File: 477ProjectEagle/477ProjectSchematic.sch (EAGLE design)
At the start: 42 parts, among them Q1 AO4419, X10 22-23-2041, X9 22-23-2041

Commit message: Updated schematic
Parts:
- removed FUELGUAGE: 22-23-2021, con-molex:22-23-2021
- removed X9: 22-23-2041, con-molex:22-23-2041
- added SW_1: RESET_BUTTON, MinotaurParts:RESET_BUTTON
- added U$19: TXB0108, MinotaurParts:TXB0108
- added U$20: 10k, MinotaurParts:R-US
- added U$21: 1k, MinotaurParts:R-US
- added U$22: (no value), MinotaurParts:R-US
- added X1: 22-23-2051, con-molex:22-23-2051
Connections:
- new net N$17: U$1.PMD3/RE3, U$19.A2
- new net N$32: U$1.PMD1/RE1, U$19.A4
- new net N$34: U$1.OC3/RD2, U$19.A5
- new net N$38: U$1.OC2/RD1, U$19.A6
- new net N$39: U$19.B1, U$2.IN1
- new net N$41: U$19.B4, U$2.IN4
- new net N$42: U$19.B2, U$2.IN2
- new net N$43: U$19.B3, U$2.IN3
- new net N$44: U$19.B5, U$2.ENA
- new net N$45: U$19.B6, U$2.ENB
- new net N$46: U$19.VCCA
- new net N$47: U$19.B7, U$39.R1OUT
- new net N$49: U$19.B8, U$39.T1IN
- new net N$50: U$39.T1OUT
- new net N$53: U$39.R1IN
- new net N$56: U$19.OE, U$20.1
- new net N$57: U$20.2
- new net N$58: U$1.*MCLR, U$21.2, U$22.1
- new net N$60: SW_1.2, U$21.1
- new net N$62: U$22.2
- net +5V: now also U$19.VCCB
- net +7V: now also U$2.VS; no longer X10-3.S, X9-3.S
- net GND: now also SW_1.1, U$1.VSS, U$1.VSS_2, U$1.VSS_3, U$19.GND, U$2.VSS
- net N$14: now also U$1.PGC1/EMUC1/VREF-/AN1/CN3/RB1; no longer U$1.VSS_2
- net N$15: now also U$1.PMD4/RE4, U$19.A1; no longer U$1.VSS
- net N$19: now also U$2.OUT2
- net N$20: now also X10-3.S; no longer X9-1.S
- net N$21: now also U$2.OUT3, X10-4.S; no longer X9-2.S
- net N$23: no longer FUELGUAGE-1.S
- net N$24: no longer FUELGUAGE-2.S
- net N$29: now also U$1.PMD2/RE2, U$19.A3; no longer U$2.VS
- net N$7: now also U$1.PGD1/EMUD1/PMA6/VREF+/AN0/CN2/RB0; no longer U$1.VSS_3
- net N$8: now also U$19.A7; no longer U$39.R1OUT
- net N$9: now also U$19.A8; no longer U$39.T1IN
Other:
- note added: "3.3Volt!"
- note added: "TO MOTORS"
- moved on the sheet: Q1, U$10, U$11, U$12, U$13, U$14, U$15, U$16, U$17, U$18, U$2, U$26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

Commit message: Fixed Schematic
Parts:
- added J1: POWER_JACKPTH, SparkFun-Connectors:POWER_JACKPTH
- added SV1: (no value), con-lsta:FE08-1
- added SV2: (no value), con-lsta:FE09-1
- added SV3, SV4: (no value), con-lsta:FE10-1
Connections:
- new net N$13: U$1.SDA1/RG3
- new net N$31: U$1.PMA8/U2TX/SCL2/CN18/RF5
- new net N$61: SV2.4, U$1.TDI/PMA10/AN13/RB13
- new net N$63: U$1.TDO/PMA12/AN11/RB11
- new net N$64: SV2.7, U$1.TMS/PMA13/CVREF/AN10/RB10
- new net N$65: U$1.*U2CTS/C1OUT/AN8/RB8
- new net N$66: U$1.PGD2/EMUD2/AN7/RB7
- new net N$67: SV4.10, U$1.*U1RTS/BCLK1/SCK1/INT0/RF6
- new net N$68: U$1.OSC1/CLKI/RC12
- new net N$69: U$1.IC1/RTCC/INT1/RD8
- new net N$70: SV4.6, U$1.IC2/*U1CTS/INT2/RD9
- new net N$71: SV4.5, U$1.IC3/PMCS2/INT3/RD10
- new net N$72: SV4.4, U$1.IC4/PMCS1/INT4/RD11
- new net N$73: SV4.3, U$1.OC1/RD0
- new net N$74: U$1.SOSCI/CN1/RC13
- new net N$75: U$1.SOSCO/T1CK/CN0/RC14
- new net N$76: SV3.1, U$1.PMD0/RE0
- new net N$77: SV3.2
- new net N$78: SV3.3
- new net N$79: SV3.4
- new net N$80: SV3.5
- new net N$81: SV3.6
- new net N$82: SV3.7, U$1.CN15/RD6
- new net N$83: SV3.8, U$1.PMRD/CN14/RD5
- new net N$84: SV3.9, U$1.PMWR/OC5/IC5/CN13/RD4
- new net N$85: SV3.10
- new net SCL: ENCODER-1.S, X1-4.S
- new net SDA: ENCODER-2.S, X1-3.S
- new net V+: J1.PWR, U$12.EN, U$12.VIN, U$13.1, U$26.VIN, U$27.1, U$28.2, U$29.1, U$30.2, U$31.1, U$32.2, U$4.VIN, U$5.1
- net +3V3: now also U$1.VDD, U$1.VDD_2, U$1.VDD_3, U$19.VCCA, U$20.2, U$22.2, X1-2.S
- net +5V: now also U$1.AVDD
- net GND: now also J1.GND, J1.GNDBREAK, U$1.AVSS, X1-1.S
- net N$10: now also SV1.7, U$1.PMD6/RE6; no longer U$12.EN, U$12.VIN, U$13.1
- net N$11: now also SV1.6, U$1.PMD7/RE7; no longer U$1.VDD_2
- net N$22: now also U$1.PMA0/AN15/OCFB/CN12/RB15
- net N$23: now also SV1.5, U$1.PMA5/SCK2/CN8/RG6; no longer ENCODER-1.S
- net N$24: now also SV1.4, U$1.PMA4/SDI2/CN9/RG7; no longer ENCODER-2.S
- net N$26: now also SV1.3, U$1.PMA3/SDO2/CN10/RG8; no longer U$26.VIN, U$27.1, U$28.2, U$29.1, U$30.2, U$31.1, U$32.2
- net N$27: now also SV1.2, U$1.PMA2/*SS2/CN11/RG9; no longer U$1.AVDD
- net N$30: now also SV1.1, U$1.PGC2/EMUC2/AN6/OCFA/RB6; no longer U$4.VIN, U$5.1
- net N$46: now also U$1.PMA9/U2RX/SDA2/CN17/RF4; no longer U$19.VCCA
- net N$5: now also U$1.PMA7/C2OUT/AN9/RB9
- net N$57: now also U$1.PMA1/*U2RTS/BCLK2/AN14/RB14; no longer U$20.2
- net N$59: now also U$1.OSC2/CLKO/RC15; no longer U$1.VDD
- net N$6: now also SV1.8, U$1.PMD5/RE5; no longer U$1.VDD_3
- net N$62: now also U$1.TCK/PMA11/AN12/RB12; no longer U$22.2
- net N$9: now also U$1.U1TX/SDO1/RF3
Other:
- note removed: "3.3Volt!"
- moved on the sheet: X1-1, X1-2, X1-3, X1-4

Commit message: Made further edits to both schematics
decoupling capacitors, values for passive components, RJ11 and SUBD
connectors.
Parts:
- added U$23, U$24, U$25, U$40, U$41, U$42, U$43, U$44: 10uF, MinotaurParts:C-US-1206
- added X2: XRJK-S-01-6-6-0-2G2-NO, con-xmultiple:XRJK-S-01-6-6-0-2G2-NO
- added X3: (no value), con-subd:F09HP
- U$11: value APXA100ARA271MJ80G -> 270uF
- U$13: value (none) -> 10uF
- U$14: value (none) -> 22uF
- U$15: value SDR0403 -> 2.2uH
- U$16: value (none) -> 100k; device MinotaurParts:R-US -> MinotaurParts:R-US"
- U$17, U$18, U$20, U$21: device MinotaurParts:R-US -> MinotaurParts:R-US"
- U$22: value (none) -> 5k; device MinotaurParts:R-US -> MinotaurParts:R-US"
- U$27, U$5: value C-US-1210 -> 10uF
- U$28: value (none) -> 110k; device MinotaurParts:R-US -> MinotaurParts:R-US"
- U$29: value (none) -> 740nF
- U$30: value (none) -> 2.55k; device MinotaurParts:R-US -> MinotaurParts:R-US"
- U$31: value (none) -> 1.0nF
- U$32: value (none) -> 0.020; device MinotaurParts:R-US -> MinotaurParts:R-US"
- U$34: value (none) -> 4.7uH
- U$35: value (none) -> 3.9nF
- U$36: value (none) -> 12k; device MinotaurParts:R-US -> MinotaurParts:R-US"
- U$37: value (none) -> 1.4k; device MinotaurParts:R-US -> MinotaurParts:R-US"
- U$38: value T495D336K025ATE090 -> 33uF
- U$6: value (none) -> 10nF
- U$7: value SRR1210 -> 12uH
- U$8: value (none) -> 10k; device MinotaurParts:R-US -> MinotaurParts:R-US"
- U$9: value (none) -> 2.05k; device MinotaurParts:R-US -> MinotaurParts:R-US"
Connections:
- removed net N$50: U$39.T1OUT
- new net N$86: X2.3
- new net N$87: U$39.R1IN, X3.3
- net +3V3: now also U$23.1, U$24.1, U$25.1, U$41.1, U$44.1, X2.2
- net +5V: now also U$15.2, U$40.1, U$42.1, U$43.1; no longer U$15.B
- net +7V: now also U$7.2; no longer U$7.A
- net GND: now also U$23.2, U$24.2, U$25.2, U$40.2, U$41.2, U$42.2, U$43.2, U$44.2, X3.1
- net N$14: now also X2.5
- net N$16: now also U$7.1; no longer U$7.B
- net N$36: now also U$15.1; no longer U$15.A
- net N$53: now also U$39.T1OUT, X3.2; no longer U$39.R1IN
- net N$58: now also X2.1
- net N$7: now also X2.4
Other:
- note added: "PIC24FJ128GA006"
- moved on the sheet: U$12, U$13, U$14, U$15, U$16, U$17, U$18, U$31, U$7

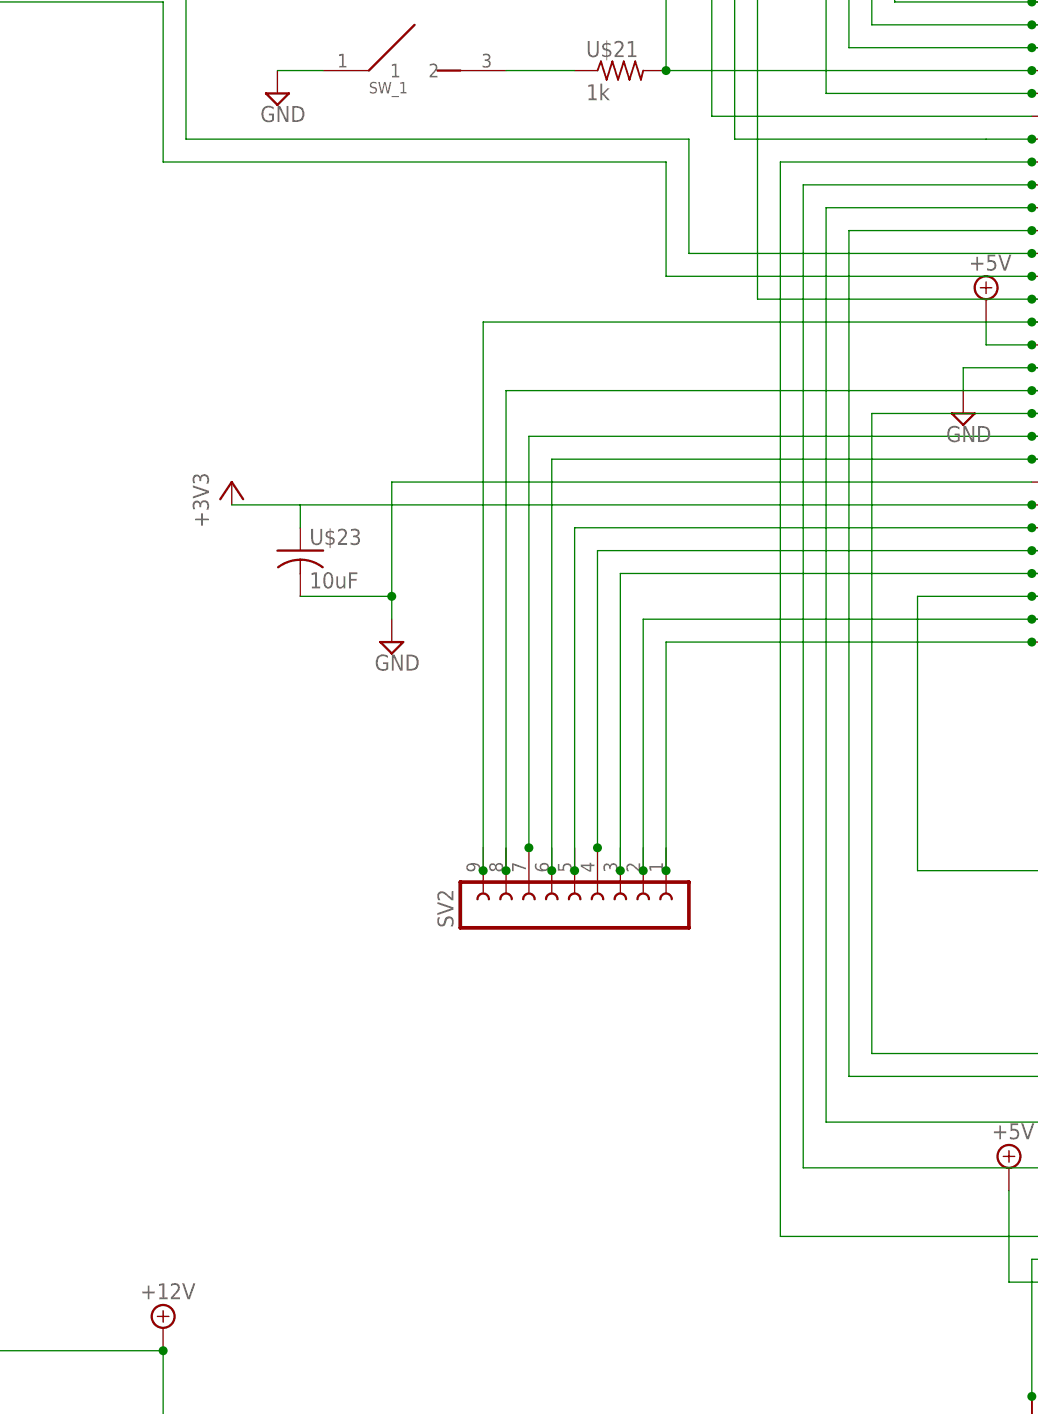
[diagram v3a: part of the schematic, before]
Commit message: Updated micro code and small schematic fix
Added ADC code to micro project. The code initializes adc to capture
data from all 5 sensors the interrupt when done.
Also added decoupling caps to the ADC input lines.
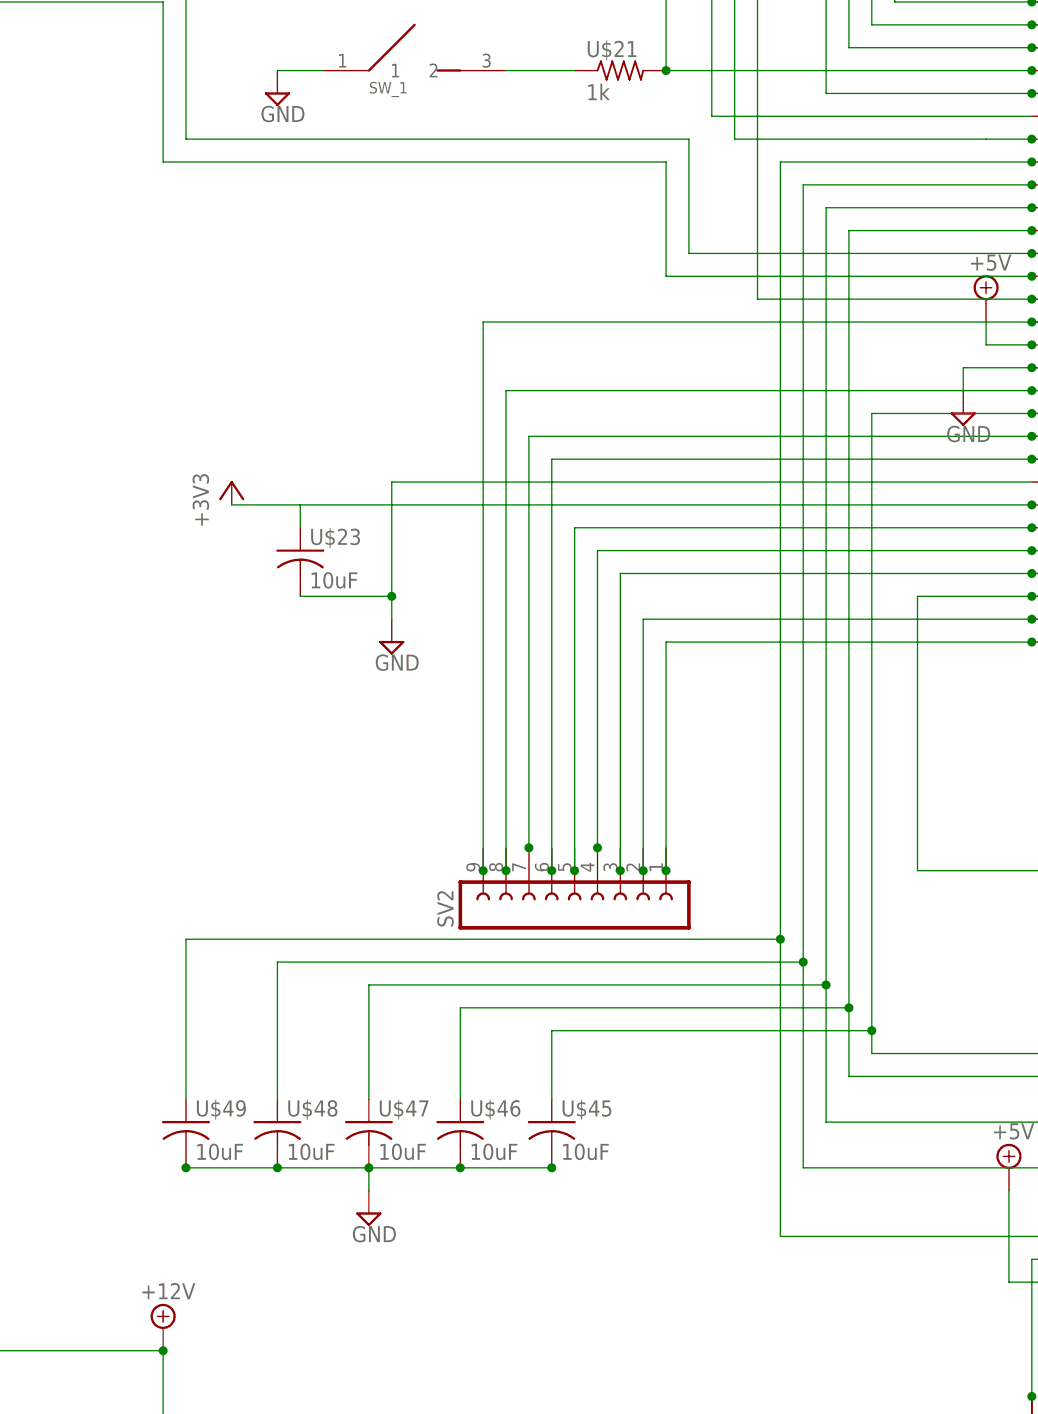
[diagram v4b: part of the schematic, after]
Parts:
- added U$45, U$46, U$47, U$48, U$49: 10uF, MinotaurParts:C-US-1206
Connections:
- net GND: now also U$45.2, U$46.2, U$47.2, U$48.2, U$49.2
- net N$1: now also U$49.1
- net N$2: now also U$48.1
- net N$3: now also U$47.1
- net N$4: now also U$46.1
- net N$5: now also U$45.1
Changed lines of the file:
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@@
 <part name="X3" library="con-subd" deviceset="F09" device="HP"/>
 <part name="SUPPLY47" library="supply2" deviceset="GND" device=""/>
+<part name="U$45" library="MinotaurParts" deviceset="C-US-1206" device="" value="10uF"/>
+<part name="U$46" library="MinotaurParts" deviceset="C-US-1206" device="" value="10uF"/>
+<part name="U$47" library="MinotaurParts" deviceset="C-US-1206" device="" value="10uF"/>
+<part name="U$48" library="MinotaurParts" deviceset="C-US-1206" device="" value="10uF"/>
+<part name="U$49" library="MinotaurParts" deviceset="C-US-1206" device="" value="10uF"/>
+<part name="SUPPLY48" library="supply2" deviceset="GND" device=""/>
 </parts>
 <sheets>
@@
 <instance part="X3" gate="G$1" x="248.92" y="25.4"/>
 <instance part="SUPPLY47" gate="GND" x="236.22" y="35.56"/>
+<instance part="U$45" gate="G$1" x="-132.08" y="-83.82"/>
+<instance part="U$46" gate="G$1" x="-142.24" y="-83.82"/>
+<instance part="U$47" gate="G$1" x="-152.4" y="-83.82"/>
+<instance part="U$48" gate="G$1" x="-162.56" y="-83.82"/>
+<instance part="U$49" gate="G$1" x="-172.72" y="-83.82"/>
+<instance part="SUPPLY48" gate="GND" x="-152.4" y="-93.98"/>
 </instances>
 <busses>
@@
 <pinref part="U$1" gate="A" pin="C1IN+/AN5/CN7/RB5"/>
 <wire x1="-78.74" y1="22.86" x2="-106.68" y2="22.86" width="0.1524" layer="91"/>
-<wire x1="-106.68" y1="22.86" x2="-106.68" y2="-96.52" width="0.1524" layer="91"/>
+<wire x1="-106.68" y1="22.86" x2="-106.68" y2="-63.5" width="0.1524" layer="91"/>
 <pinref part="SENSOR1" gate="-1" pin="S"/>
+<wire x1="-106.68" y1="-63.5" x2="-106.68" y2="-96.52" width="0.1524" layer="91"/>
 <wire x1="-106.68" y1="-96.52" x2="-76.2" y2="-96.52" width="0.1524" layer="91"/>
 <junction x="-76.2" y="-96.52"/>
 <junction x="-78.74" y="22.86"/>
+<pinref part="U$49" gate="G$1" pin="1"/>
+<wire x1="-106.68" y1="-63.5" x2="-172.72" y2="-63.5" width="0.1524" layer="91"/>
+<wire x1="-172.72" y1="-63.5" x2="-172.72" y2="-81.28" width="0.1524" layer="91"/>
+<junction x="-106.68" y="-63.5"/>
 </segment>
 </net>
@@
 <wire x1="-55.88" y1="-96.52" x2="-55.88" y2="-88.9" width="0.2032" layer="91"/>
 <wire x1="-55.88" y1="-88.9" x2="-104.14" y2="-88.9" width="0.1524" layer="91"/>
-<wire x1="-104.14" y1="-88.9" x2="-104.14" y2="20.32" width="0.1524" layer="91"/>
+<wire x1="-104.14" y1="-88.9" x2="-104.14" y2="-66.04" width="0.1524" layer="91"/>
 <pinref part="U$1" gate="A" pin="C1IN-/AN4/CN6/RB4"/>
+<wire x1="-104.14" y1="-66.04" x2="-104.14" y2="20.32" width="0.1524" layer="91"/>
 <wire x1="-104.14" y1="20.32" x2="-78.74" y2="20.32" width="0.1524" layer="91"/>
 <junction x="-55.88" y="-96.52"/>
 <junction x="-78.74" y="20.32"/>
+<pinref part="U$48" gate="G$1" pin="1"/>
+<wire x1="-104.14" y1="-66.04" x2="-162.56" y2="-66.04" width="0.1524" layer="91"/>
+<wire x1="-162.56" y1="-66.04" x2="-162.56" y2="-81.28" width="0.1524" layer="91"/>
+<junction x="-104.14" y="-66.04"/>
 </segment>
 </net>
@@
 <pinref part="U$1" gate="A" pin="C2IN+/AN3/CN5/RB3"/>
 <wire x1="-78.74" y1="17.78" x2="-101.6" y2="17.78" width="0.1524" layer="91"/>
-<wire x1="-101.6" y1="17.78" x2="-101.6" y2="-83.82" width="0.1524" layer="91"/>
+<wire x1="-101.6" y1="17.78" x2="-101.6" y2="-68.58" width="0.1524" layer="91"/>
+<wire x1="-101.6" y1="-68.58" x2="-101.6" y2="-83.82" width="0.1524" layer="91"/>
 <wire x1="-101.6" y1="-83.82" x2="-38.1" y2="-83.82" width="0.1524" layer="91"/>
 <wire x1="-38.1" y1="-83.82" x2="-38.1" y2="-96.52" width="0.2032" layer="91"/>
@@
 <junction x="-78.74" y="17.78"/>
 <junction x="-35.56" y="-96.52"/>
+<pinref part="U$47" gate="G$1" pin="1"/>
+<wire x1="-152.4" y1="-68.58" x2="-152.4" y2="-81.28" width="0.1524" layer="91"/>
+<wire x1="-101.6" y1="-68.58" x2="-152.4" y2="-68.58" width="0.1524" layer="91"/>
+<junction x="-101.6" y="-68.58"/>
 </segment>
 </net>
@@
 <wire x1="-15.24" y1="-96.52" x2="-15.24" y2="-78.74" width="0.2032" layer="91"/>
 <wire x1="-15.24" y1="-78.74" x2="-99.06" y2="-78.74" width="0.1524" layer="91"/>
-<wire x1="-99.06" y1="-78.74" x2="-99.06" y2="15.24" width="0.1524" layer="91"/>
+<wire x1="-99.06" y1="-78.74" x2="-99.06" y2="-71.12" width="0.1524" layer="91"/>
 <pinref part="U$1" gate="A" pin="C2IN-/AN2/*SS1/CN4/RB2"/>
+<wire x1="-99.06" y1="-71.12" x2="-99.06" y2="15.24" width="0.1524" layer="91"/>
 <wire x1="-99.06" y1="15.24" x2="-78.74" y2="15.24" width="0.1524" layer="91"/>
 <junction x="-15.24" y="-96.52"/>
 <junction x="-78.74" y="15.24"/>
+<pinref part="U$46" gate="G$1" pin="1"/>
+<wire x1="-142.24" y1="-71.12" x2="-142.24" y2="-81.28" width="0.1524" layer="91"/>
+<wire x1="-99.06" y1="-71.12" x2="-142.24" y2="-71.12" width="0.1524" layer="91"/>
+<junction x="-99.06" y="-71.12"/>
 </segment>
 </net>
@@
 <wire x1="-76.2" y1="-5.08" x2="-78.74" y2="-5.08" width="0.1524" layer="91"/>
 <wire x1="-78.74" y1="-5.08" x2="-96.52" y2="-5.08" width="0.1524" layer="91"/>
-<wire x1="-96.52" y1="-5.08" x2="-96.52" y2="-76.2" width="0.1524" layer="91"/>
+<wire x1="-96.52" y1="-5.08" x2="-96.52" y2="-73.66" width="0.1524" layer="91"/>
+<wire x1="-96.52" y1="-73.66" x2="-96.52" y2="-76.2" width="0.1524" layer="91"/>
 <wire x1="-96.52" y1="-76.2" x2="2.54" y2="-76.2" width="0.1524" layer="91"/>
 <wire x1="2.54" y1="-76.2" x2="2.54" y2="-96.52" width="0.2032" layer="91"/>
@@
 <pinref part="U$1" gate="A" pin="PMA7/C2OUT/AN9/RB9"/>
 <junction x="-78.74" y="-5.08"/>
+<pinref part="U$45" gate="G$1" pin="1"/>
+<wire x1="-132.08" y1="-73.66" x2="-132.08" y2="-81.28" width="0.1524" layer="91"/>
+<wire x1="-96.52" y1="-73.66" x2="-132.08" y2="-73.66" width="0.1524" layer="91"/>
+<junction x="-96.52" y="-73.66"/>
 </segment>
 </net>
@@
 <pinref part="SUPPLY47" gate="GND" pin="GND"/>
 </segment>
-</net>
+<segment>
+<pinref part="U$45" gate="G$1" pin="2"/>
+<pinref part="U$49" gate="G$1" pin="2"/>
+<wire x1="-132.08" y1="-88.9" x2="-142.24" y2="-88.9" width="0.1524" layer="91"/>
+<wire x1="-142.24" y1="-88.9" x2="-152.4" y2="-88.9" width="0.1524" layer="91"/>
+<wire x1="-152.4" y1="-88.9" x2="-162.56" y2="-88.9" width="0.1524" layer="91"/>
+<wire x1="-162.56" y1="-88.9" x2="-172.72" y2="-88.9" width="0.1524" layer="91"/>
+<wire x1="-152.4" y1="-88.9" x2="-152.4" y2="-91.44" width="0.1524" layer="91"/>
+<pinref part="SUPPLY48" gate="GND" pin="GND"/>
+<pinref part="U$46" gate="G$1" pin="2"/>
+<junction x="-142.24" y="-88.9"/>
+<junction x="-132.08" y="-88.9"/>
+<pinref part="U$47" gate="G$1" pin="2"/>
+<junction x="-152.4" y="-88.9"/>
+<pinref part="U$48" gate="G$1" pin="2"/>
+<junction x="-162.56" y="-88.9"/>
+<junction x="-172.72" y="-88.9"/>
+</segment>
+</net>
